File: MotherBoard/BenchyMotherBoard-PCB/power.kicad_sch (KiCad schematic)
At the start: 203 parts, among them J1 PWR-CONN, U1 STM32MP157FAB1, U10 USB7206C, U2 TPS65400RGZT, U3 NCP51200, U4 ATTINY416-MNR, U5 TLV3401, U6 MAX15027, U7 SN74LVC1G32, U8 74HCT2G08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

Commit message: Add volt meter PCB
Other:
- note added: "1.8V REGULATOR DETECT"
- note added: "ALWAYS ON"
- note added: "ANALOG REGULATOR"
- note added: "Analog Supply"
- note added: "DDR MEMORY REGULATOR"
- note added: "Digital Supply From Power Supply (Used for power Supply Control)"
- note added: "High Voltage Supply From External SMPS (Display Backlight)"
- note added: "MAIN POWER CONTROLLER"
- note added: "MOUNTS"
- note added: "Main Digital Supply"
- note added: "POWER CTRL & INDICATORS"
- note added: "POWER SEQUENCE"
- note added: "RUN"
- note added: "SIC451 Supply From PowerSupply PCB"
- note added: "SMPS POWER INPUT"
- note added: "START"
- note added: "STM32 MPU POWER"
- note added: "USB HUB POWER"
- note added: "USB Hub PHY Layer Supply"
- note added: "USB VDD REGULATOR"
- note added: "VDD-PWR"
- note removed: "2.5V-3.3V"
- note removed: "Analog Adjustable Reference"
- note removed: "Analog Main Supply"
- note removed: "High Voltage Supply For The Display Backlight"
- note removed: "Main Supply"
- note removed: "SIC451 Supply For General Purpose Use"
- note removed: "Supply For the USB PHY"
- note removed: "VREF"
- moved on the sheet: C1, C10, C11, C12, C13, C14, C15, C16, C17, C18, C182, C183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

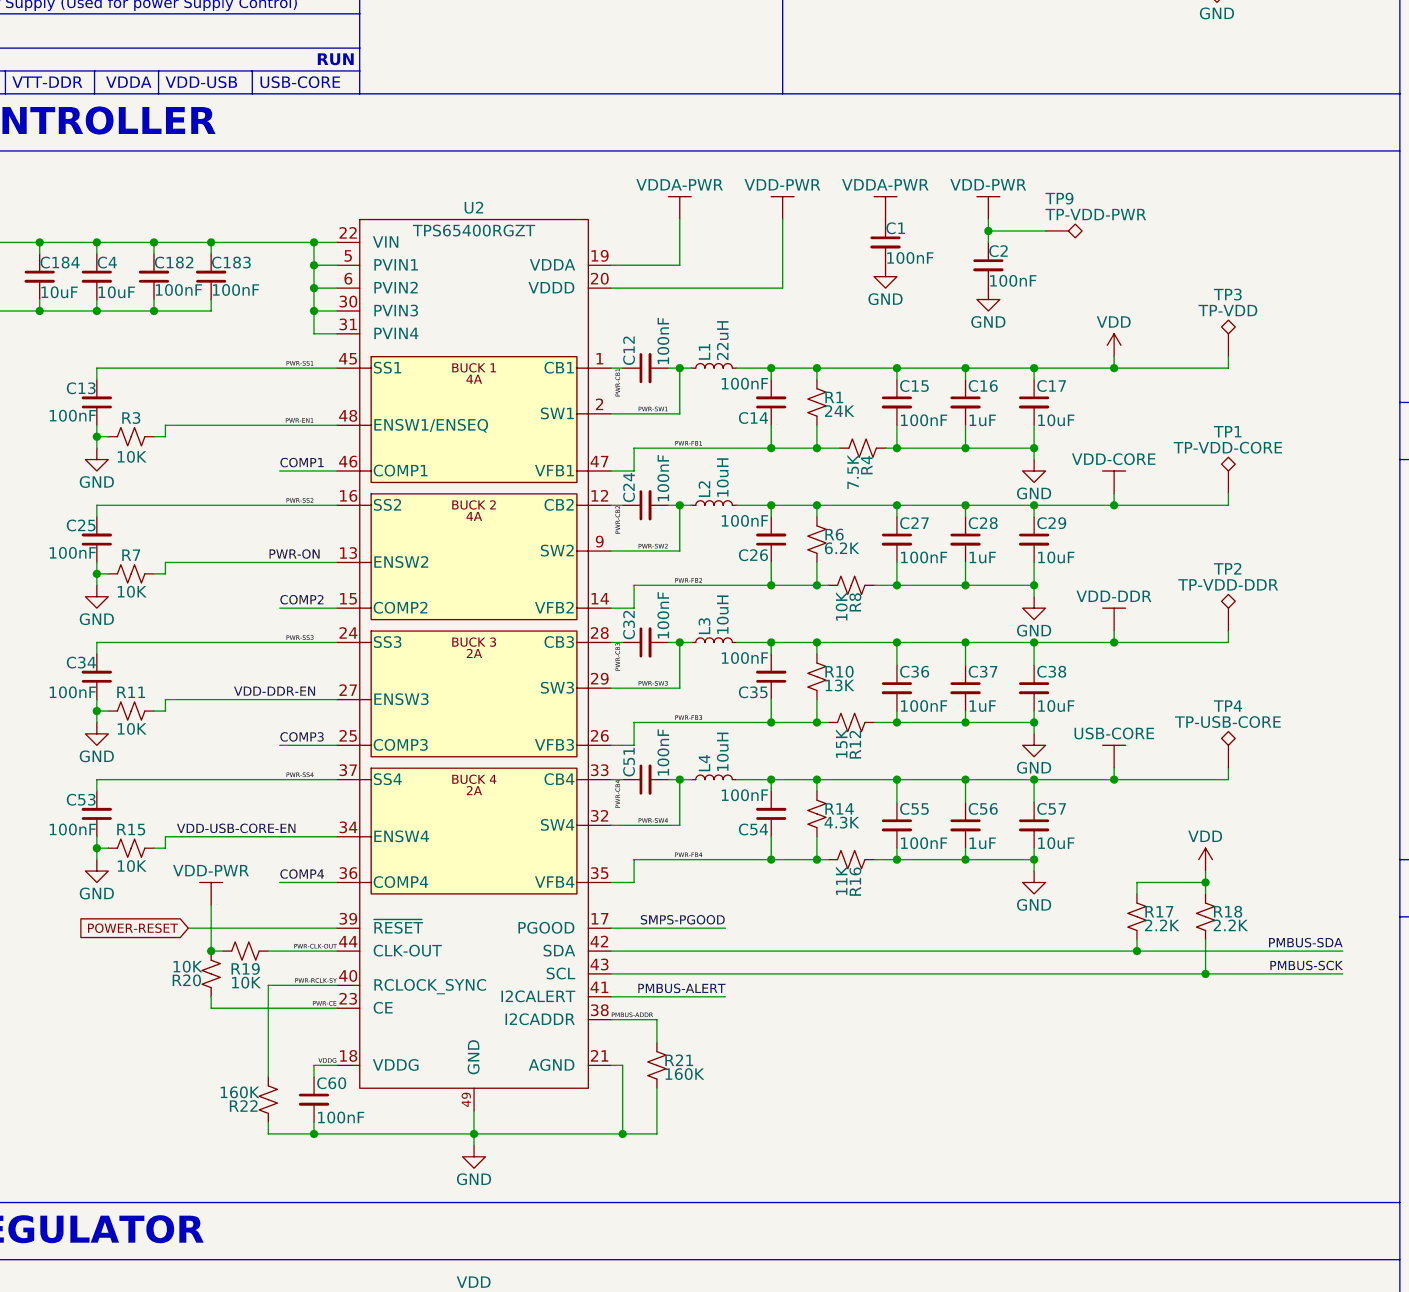
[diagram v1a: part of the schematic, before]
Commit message: Fix schematic bugs and add PIO firmware (Not Working)
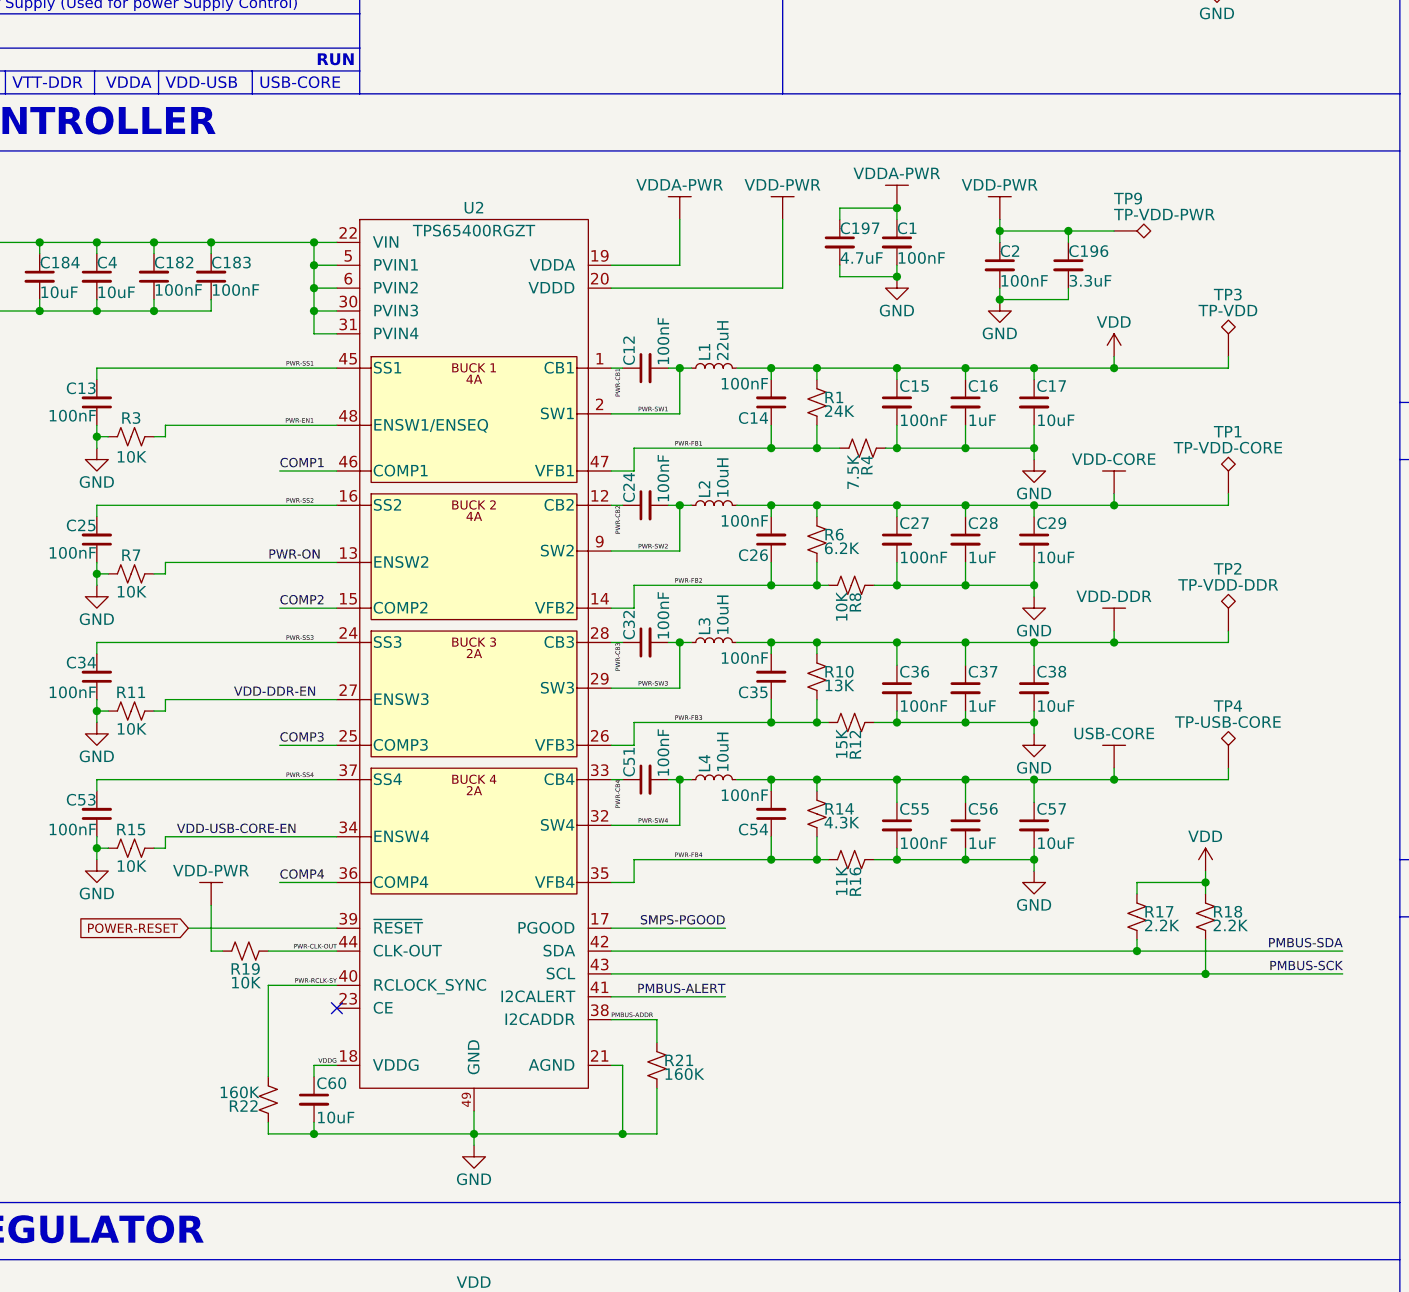
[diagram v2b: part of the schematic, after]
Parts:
- removed R20: 10K, Resistor_SMD:R_0402_1005Metric, symbol Device:R_Small_US
- added C196: 3.3uF, Capacitor_SMD:C_0603_1608Metric, symbol Device:C_Small
- added C197: 4.7uF, Capacitor_SMD:C_0603_1608Metric, symbol Device:C_Small
- C60: value 100nF -> 10uF; footprint Capacitor_SMD:C_0402_1005Metric -> Capacitor_SMD:C_0805_2012Metric
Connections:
- net GND: now also C196.2, C197.2
- net VDD-PWR: now also C196.1
- net VDDA-PWR: now also C197.1
- net PWR-CE: no longer names the net of U2.23 (CE)
- no-connect marks 3 -> 4
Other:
- moved on the sheet: C1, C2, TP9

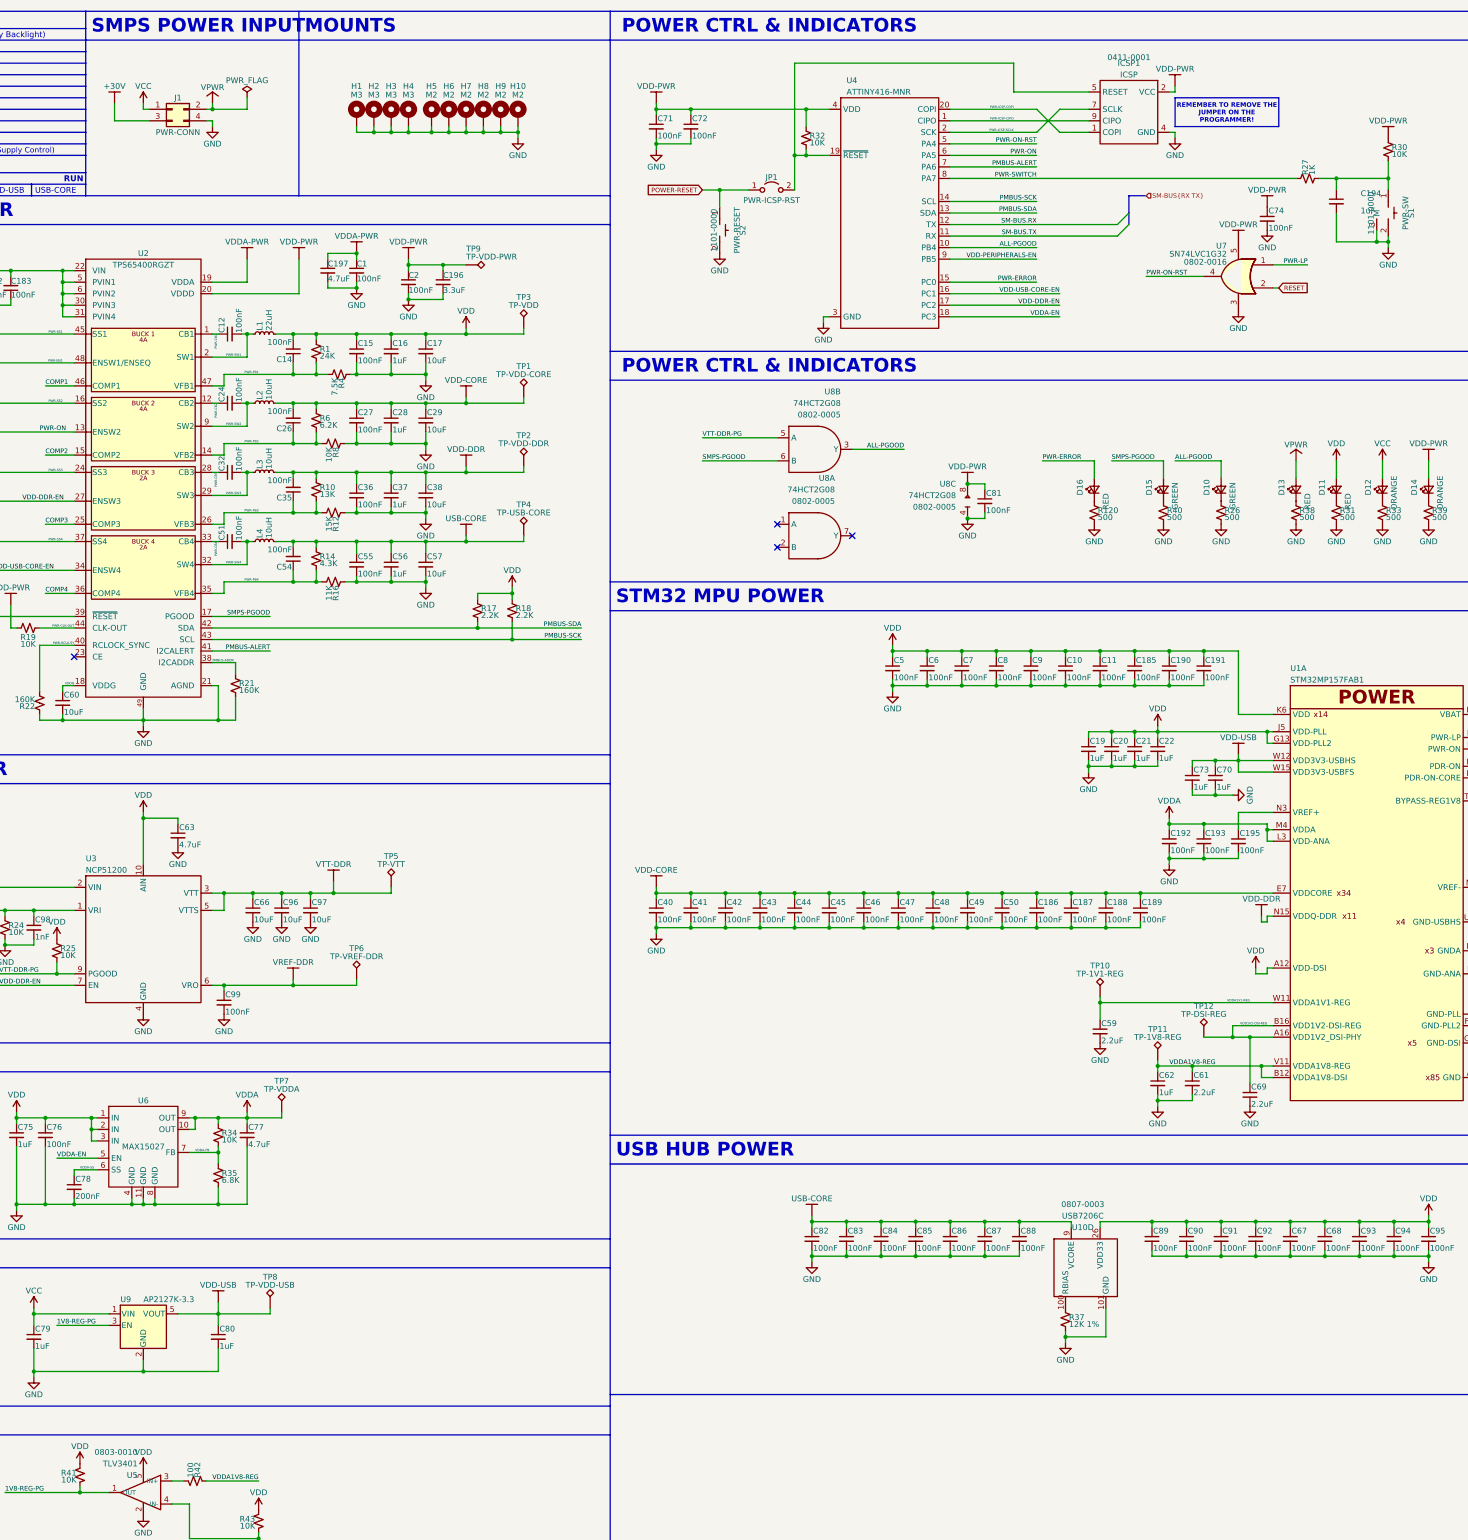
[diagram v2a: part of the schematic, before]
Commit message: Add mplab config and proj / remove pio proj
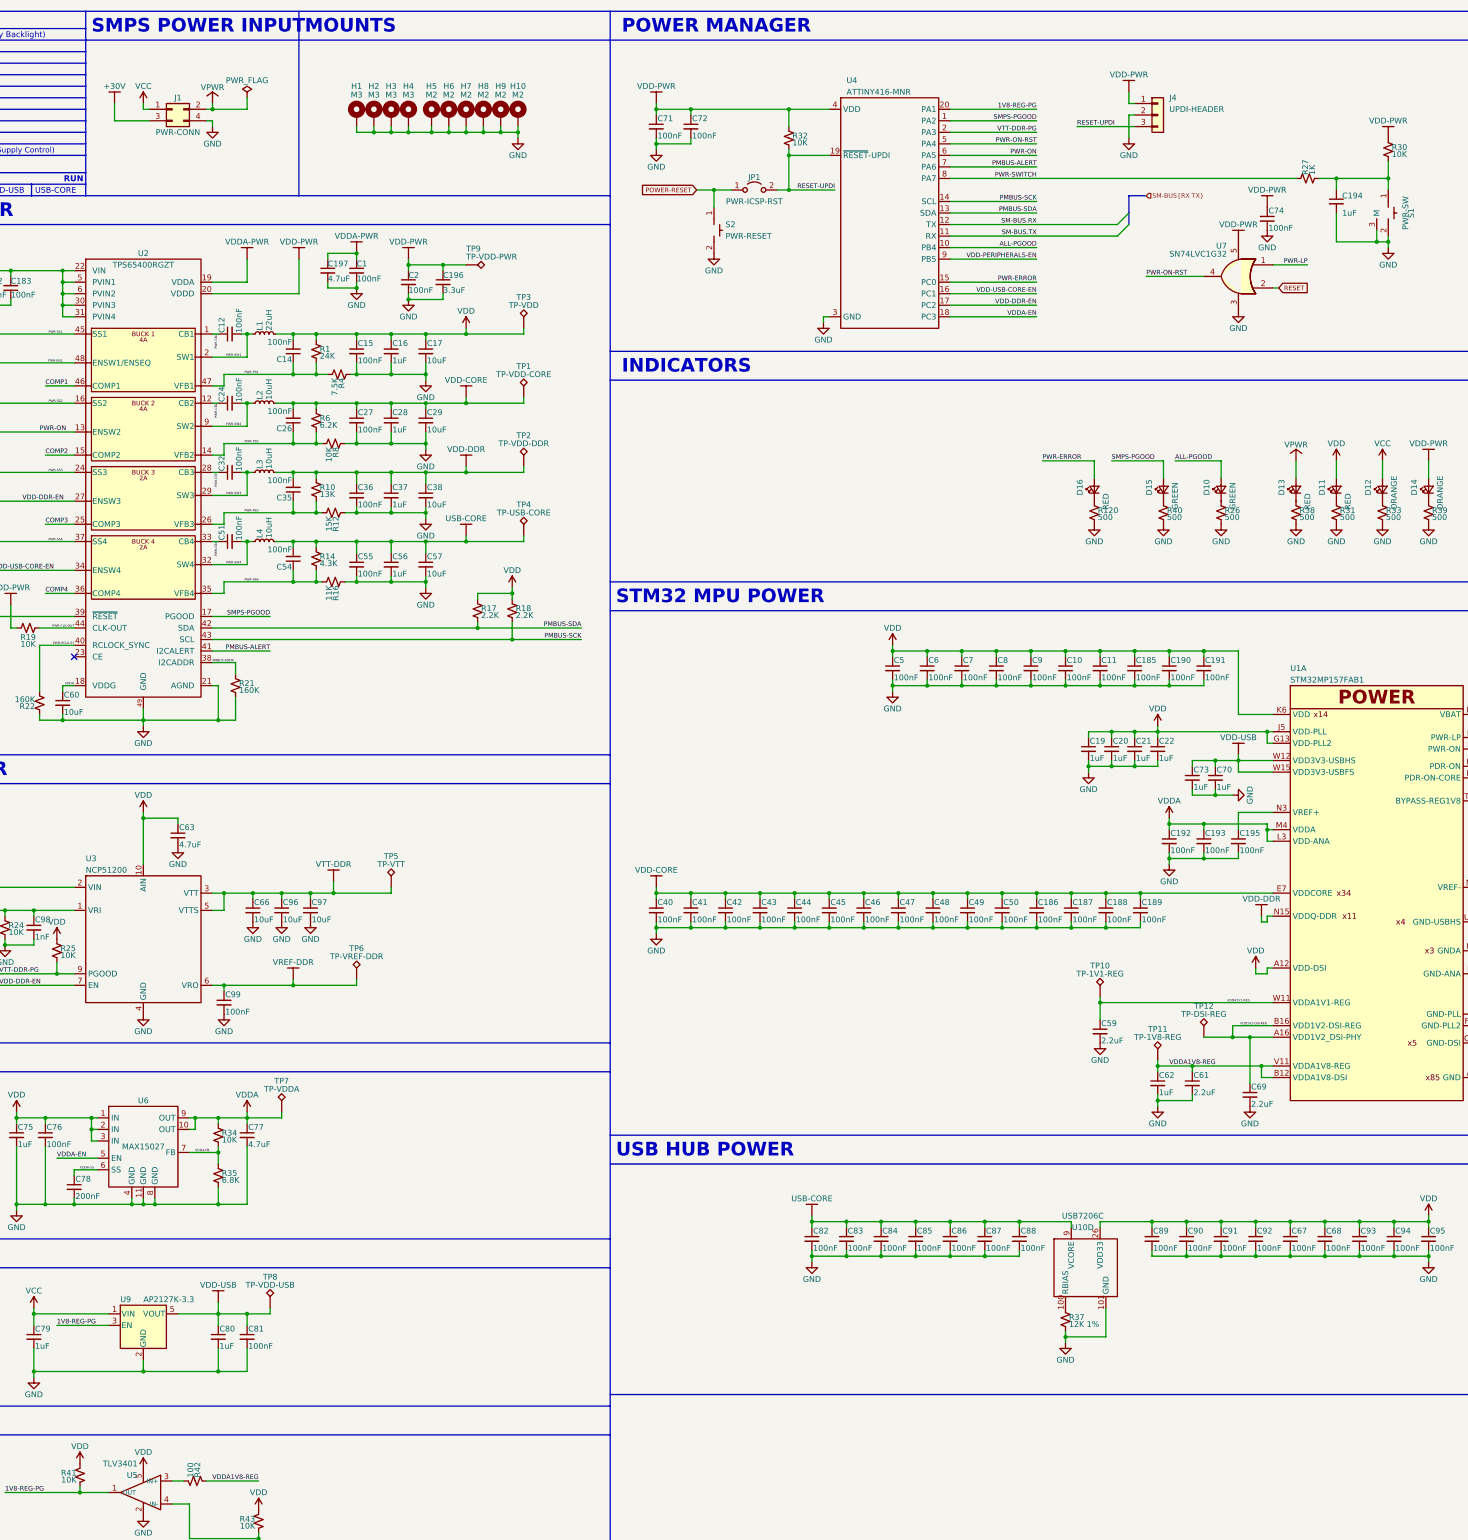
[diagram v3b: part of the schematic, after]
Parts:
- removed ICSP1: ICSP, Connector:Tag-Connect_TC2050-IDC-FP_2x05_P1.27mm_Vertical, symbol Daxxn_Connectors:ICSP
- removed U8: 74HCT2G08, Package_SO:TSSOP-8_3x3mm_P0.65mm, symbol Daxxn_Logic:74HCT2G08
- added J4: UPDI-HEADER, Connector_PinHeader_2.54mm:PinHeader_1x03_P2.54mm_Vertical, symbol Connector_Generic:Conn_01x03
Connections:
- net PWR-ICSP-CIPO is gone; now on net SMPS-PGOOD: U4.1 (PA2)
- net PWR-ICSP-COPI is gone; now on net 1V8-REG-PG: U4.20 (PA1)
- net PWR-ICSP-SCLK is gone; now on net VTT-DDR-PG: U4.2 (PA3)
- net GND: now also J4.2 (Pin_2)
- net VDD-PWR: now also J4.1 (Pin_1); no longer C81.1
- net VDD-USB: now also C81.1
- net RESET-UPDI: now reaches JP1.2 (B), R32.2, U4.19 (~{RESET})
- net RESET-UPDI: now also J4.3 (Pin_3)
- no-connect marks 4 -> 1
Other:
- note added: "INDICATORS"
- note added: "POWER MANAGER"
- note removed: "POWER CTRL & INDICATORS"
- moved on the sheet: JP1, R32, S2

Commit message: Fix issues with power supply schematic
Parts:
- removed R11, R15, R43, R7: 10K, Resistor_SMD:R_0402_1005Metric, symbol Device:R_Small_US
- removed R119: 4.7K, Resistor_SMD:R_0402_1005Metric, symbol Device:R_Small_US
- removed R42: 100, Resistor_SMD:R_0402_1005Metric, symbol Device:R_Small_US
- removed U4: ATTINY416-MNR, Daxxn_Packages:QFN-20-1EP_3x3mm_P0.4mm_EP1.65x1.65mm, symbol Daxxn_MicroControllers:ATTINY416-MNR
- removed U5: TLV3401, Package_TO_SOT_SMD:SOT-23-5, symbol Daxxn_OPAMP:TLV3401
- added C198, C199, C200: 100nF, Capacitor_SMD:C_0402_1005Metric, symbol Device:C_Small
- added D21: BZX584C3V3_R1, Diode_SMD:D_SOD-523, symbol Daxxn_Device:D_Zener
- added R20: 10K, Resistor_SMD:R_0402_1005Metric, symbol Device:R_Small_US
- added U4: ATTINY1606-MNR, Daxxn_Packages:QFN-20-1EP_3x3mm_P0.4mm_EP1.5x1.5mm, symbol Daxxn_MicroControllers:ATTINY1606-MNR
- R21: value 160K -> 10K
- R3, R32: value 10K -> 22K
- R41: value 10K -> 1K
- U2: footprint Package_DFN_QFN:QFN-48-1EP_7x7mm_P0.5mm_EP5.15x5.15mm_ThermalVias -> Daxxn_Packages:VQFN-48-1EP_7x7mm_P0.5mm_EP5.15x5.15mm_ThermalVias
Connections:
- net ALL-PGOOD is gone; now on net PWR-ON-RST: D10.2 (A)
- net GND: now also C198.2, C199.2, C200.2, D21.2 (A), U4.21 (GND), U4.3 (GND); no longer R3.2
- net PMBUS-SCK: now also U4.14 (PB0)
- net PMBUS-SDA: now also U4.13 (PB1)
- net POWER-RESET: now also R3.2, R41.2, D21.1 (K); no longer JP1.1 (A), S2.1
- net PWR-ERROR: now also U4.15 (PC0)
- net PWR-ON: now also U4.6 (PA5); no longer U2.13 (ENSW2)
- net PWR-ON-RST: now also U4.5 (PA4)
- net PWR-SWITCH: now also U4.9 (PB5)
- net RESET-UPDI: now also S2.1, U4.19 (~{RESET})
- net SM-BUS.RX: now also U4.12 (PB2)
- net SM-BUS.TX: now also U4.11 (PB3)
- net SMPS-PGOOD: now also U4.1 (PA2)
- net USB-CORE: now also C200.1
- net VDD: now also R20.1; no longer R17.1, R18.1, R41.1
- net VDD-CORE: now also C199.1
- net VDD-DDR-EN: now also U4.16 (PC1); no longer U2.27 (ENSW3)
- net VDD-PWR: now also R17.1, R18.1, R3.1, C198.1, U4.4 (VDD)
- net VDDA-EN: now also R20.2
- net VDDA1V8-REG: now also U4.8 (PA7)
- net VTT-DDR-PG: now also U4.17 (PC2)
- net 1V8-REG-PG renamed VDD-USB-EN
- net VDD-USB-EN: now also U4.20 (PA1); no longer R41.2
- net PMBUS-ALERT: no longer names the net of U2.41 (I2CALERT)
- net PWR-EN1: no longer names the net of U2.48 (ENSW1/ENSEQ)
- net PWR-EN1: no longer R3.1
- net VDD-USB-CORE-EN: no longer names the net of U2.34 (ENSW4)
- new net: JP1.1 (A), R41.1
- no-connect marks 1 -> 10
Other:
- note added: "ADDRESS: 0x69"
- note removed: "1.8V REGULATOR DETECT"
- moved on the sheet: C13, C194, C25, C27, C28, C29, C34, C53, C55, C56, C57, C71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
